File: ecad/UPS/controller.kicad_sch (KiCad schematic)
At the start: 36 parts, among them J4 PROG, U4 STM32L152RCT6, U5 AP2112K-3.3TRG1, U6 BOOT0, U7 NRST

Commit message: Thermistor changes
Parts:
- D10, D6, D8, D9: DESCRIPTION Standard LEDs - SMD RED DIFFUSED -> (none)

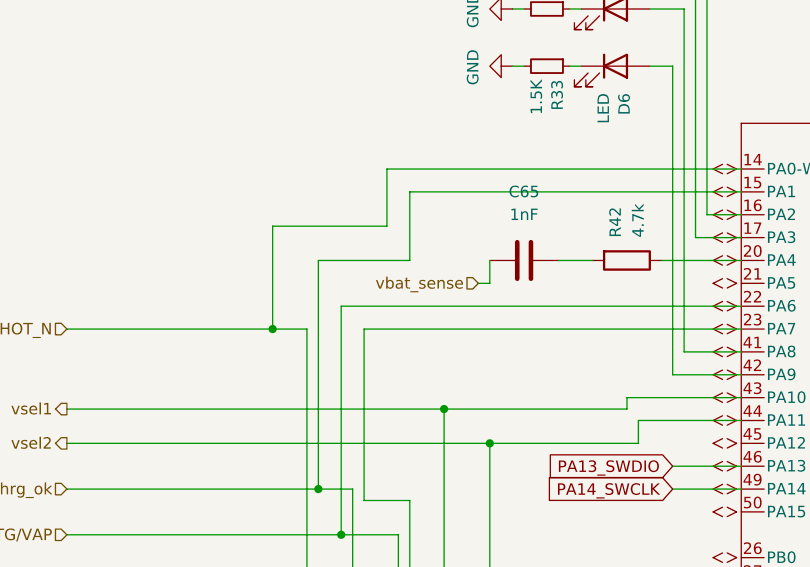
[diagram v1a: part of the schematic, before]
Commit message: Moved batteries to back, experimenting with different layouts
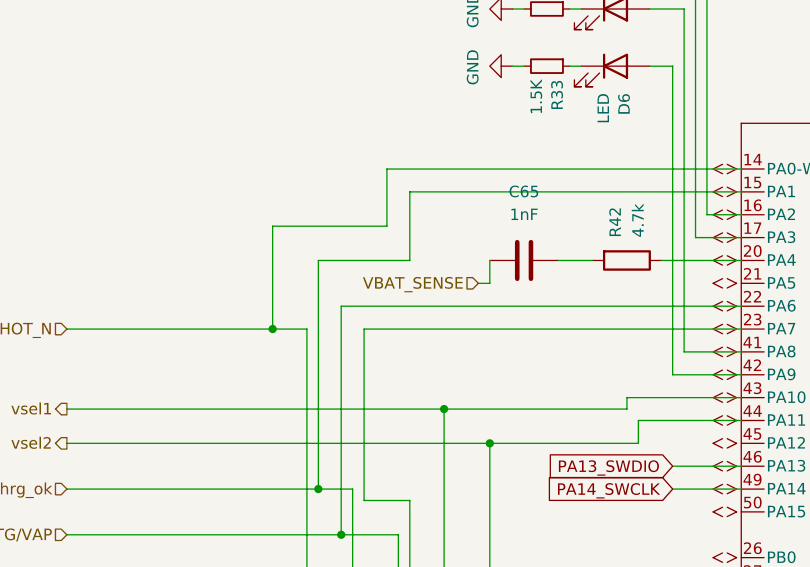
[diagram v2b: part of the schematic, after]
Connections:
- net vbat_sense renamed VBAT_SENSE
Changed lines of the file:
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@@
 		)
 	)
-	(hierarchical_label "vbat_sense"
+	(hierarchical_label "VBAT_SENSE"
 		(shape input)
 		(at 77.47 58.42 180)
